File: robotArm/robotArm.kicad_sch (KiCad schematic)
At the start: 30 parts, among them J1 Barrel_Jack, J2 Conn_01x16_Pin, J3 Conn_01x04, J4 Conn_01x04, J5 Conn_01x04, J6 Conn_01x04, U2 TMC2209_SILENTSTEPSTICK, U4 TMC2209_SILENTSTEPSTICK, U5 TMC2209_SILENTSTEPSTICK, U6 74HC165

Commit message: First Real Cleanup
First real cleanup
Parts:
- removed D1: DIAG1, LED_THT:LED_D3.0mm_FlatTop, symbol Device:LED
- removed D2: DIAG2, LED_THT:LED_D3.0mm_FlatTop, symbol Device:LED
- removed D3: DIAG3, LED_THT:LED_D3.0mm_FlatTop, symbol Device:LED
- removed D4: DIAG4, LED_THT:LED_D3.0mm_FlatTop, symbol Device:LED
- removed D5: IX1, LED_THT:LED_D3.0mm_FlatTop, symbol Device:LED
- removed D6: IX2, LED_THT:LED_D3.0mm_FlatTop, symbol Device:LED
- removed D7: IX3, LED_THT:LED_D3.0mm_FlatTop, symbol Device:LED
- removed D8: IX4, LED_THT:LED_D3.0mm_FlatTop, symbol Device:LED
- removed J2: Conn_01x16_Pin, Connector_PinHeader_2.54mm:PinHeader_1x16_P2.54mm_Vertical, symbol Connector:Conn_01x16_Pin
- removed R1: R, Resistor_THT:R_Axial_DIN0204_L3.6mm_D1.6mm_P2.54mm_Vertical, symbol Device:R
- removed R2: R, Resistor_THT:R_Box_L8.4mm_W2.5mm_P5.08mm, symbol Device:R
- removed R3, R4, R5, R6, R7, R8, R9: 330, Resistor_THT:R_Box_L8.4mm_W2.5mm_P5.08mm, symbol Device:R
- removed U6: 74HC165, Package_DIP:DIP-16_W7.62mm, symbol 74xx:74HC165
- J3: value Conn_01x04 -> STEPPER1
- J5: value Conn_01x04 -> STEPPER2
- J6: value Conn_01x04 -> STEPPER3
- U1, U2: symbol TMC2209_SILENTSTEPSTICK:TMC2209_SILENTSTEPSTICK -> Robot_Controller:Module_TMC2209
- U4: value TMC2209_SILENTSTEPSTICK -> TMC2209_MODULE; symbol TMC2209_SILENTSTEPSTICK:TMC2209_SILENTSTEPSTICK -> Robot_Controller:Module_TMC2209
- U5: value TMC2209_SILENTSTEPSTICK -> TMC2209 Module; symbol TMC2209_SILENTSTEPSTICK:TMC2209_SILENTSTEPSTICK -> Robot_Controller:Module_TMC2209
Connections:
- net +3.3V: no longer U2.15 (MS1), U4.14 (MS2), U4.15 (MS1), U5.14 (MS2)
- net EN_DRV: no longer U1.16 (~{EN}), U2.16 (~{EN}), U4.16 (~{EN}), U5.16 (~{EN})
- net GND: no longer U2.1 (GND), U2.7 (GND)
- net B1-DRV4: now reaches J4.4 (2B)
- net B1-DRV4: now also U4.4 (B1); no longer U4.3 (M1B)
- removed net DIAG1: U1.18 (DIAG)
- removed net DIAG2: U5.18 (DIAG)
- removed net DIAG3: U2.18 (DIAG)
- removed net DIAG4: U4.18 (DIAG)
- removed net IX1: U1.17 (INDEX)
- removed net IX2: U5.17 (INDEX)
- removed net IX3: U2.17 (INDEX)
- removed net IX4: U4.17 (INDEX)
- net M1-1A renamed A1-DRV1
- net A1-DRV1: now also U1.5 (A1); no longer U1.4 (M1A)
- net M1-1B renamed B1-DRV1
- net B1-DRV1: now also U1.4 (B1); no longer U1.3 (M1B)
- net M1-2A renamed A2-DRV1
- net A2-DRV1: now also U1.6 (A2); no longer U1.5 (M2A)
- net M1-2B renamed B2-DRV1
- net B2-DRV1: now also U1.3 (B2); no longer U1.6 (M2B)
- net M2-1A renamed A1-DRV2
- net A1-DRV2: now also U5.5 (A1); no longer U5.4 (M1A)
- net M2-1B renamed B1-DRV2
- net B1-DRV2: now also U5.4 (B1); no longer U5.3 (M1B)
- net M2-2A renamed A2-DRV2
- net A2-DRV2: now also U5.6 (A2); no longer U5.5 (M2A)
- net M2-2B renamed B2-DRV2
- net B2-DRV2: now also U5.3 (B2); no longer U5.6 (M2B)
- net M3-1A renamed A1-DRV3
- net A1-DRV3: now also U2.5 (A1); no longer U2.4 (M1A)
- net M3-1B renamed B1-DRV3
- net B1-DRV3: now also U2.4 (B1); no longer U2.3 (M1B)
- net M3-2A renamed A2-DRV3
- net A2-DRV3: now also U2.6 (A2); no longer U2.5 (M2A)
- net M3-2B renamed B2-DRV3
- net B2-DRV3: now also U2.3 (B2); no longer U2.6 (M2B)
- net M4-1A renamed A1-DRV4
- net A1-DRV4: now also U4.5 (A1); no longer U4.4 (M1A)
- net M4-1B renamed A2-DRV4
- net A2-DRV4: now also J4.2 (1A); no longer J4.1 (1B)
- removed net M4-2A: J4.2 (1A), U4.5 (M2A)
- new net: U2.1 (GND), U2.7 (GND)
- new net B2-DRV4: J4.1 (1B), U4.3 (B2)
- new net EN_DRV1: U1.16 (EN)
- new net EN_DRV2: U5.16 (EN)
- new net EN_DRV3: U2.16 (EN)
- new net EN_DRV4: U4.16 (EN)
- no-connect marks 27 -> 18
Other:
- added sheet Endstop Section (endstop_section.kicad_sch)
- company: (none) -> Turnimator Cyberdelix - Jan Atle Ramsli
- title: (none) -> Robot Control Board
- moved on the sheet: J3, J4, J5, J6, U7

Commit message: Attempt 2.1
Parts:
- added C4: 100μ, Capacitor_THT:CP_Radial_D7.5mm_P2.50mm, symbol Device:C
- added D9: LED, LED_THT:LED_D5.0mm_Clear, symbol Device:LED
- added J2: ENDSTOP INPUTS, Connector_PinHeader_2.54mm:PinHeader_1x16_P2.54mm_Vertical, symbol Connector:Conn_01x16_Pin
- added R1: 470 Ω, Resistor_THT:R_Axial_DIN0207_L6.3mm_D2.5mm_P2.54mm_Vertical, symbol Device:R
- added SW1: SW_DIP_x08, Package_DIP:DIP-16_W7.62mm, symbol Switch:SW_DIP_x08
- added SW2: SW_SPDT, SS-12D10G5_XKB, symbol 2026-09-22_07-48-55:SS-12D10G5
- J4: value Conn_01x04 -> STEPPER4
- U7: footprint ESP32_30pin -> Library:ESP32_30pin
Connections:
- net +12V: now also R1.1, SW2.2; no longer J1.1
- net +3.3V: now also C4.1, SW1.1, SW1.2, SW1.3, SW1.4, SW1.5, SW1.6, SW1.7, SW1.8
- net GND: now also U1.11 (CLK), U2.1 (GND), U2.11 (CLK), U2.7 (GND), U4.11 (CLK), U5.11 (CLK), C4.2, D9.2 (A), J2.10 (Pin_10), J2.12 (Pin_12), J2.14 (Pin_14), J2.16 (Pin_16), J2.2 (Pin_2), J2.4 (Pin_4), J2.6 (Pin_6), J2.8 (Pin_8)
- net MS1-DRV4: now reaches U4.14 (MS2)
- net MS1-DRV4: now also SW1.10
- net MS2-DRV4: now reaches U4.15 (MS1)
- net MS2-DRV4: now also SW1.9
- net MS2-DRV2: now reaches U5.14 (MS2)
- net MS2-DRV2: now also SW1.13
- net MS1-DRV2: now reaches U5.15 (MS1)
- net MS1-DRV2: now also SW1.14
- net MS2-DRV1: now reaches U1.14 (MS2)
- net MS2-DRV1: now also SW1.15
- net MS1-DRV1: now reaches U1.15 (MS1)
- net MS1-DRV1: now also SW1.16
- net MS2-DRV3: now reaches U2.14 (MS2)
- net MS2-DRV3: now also SW1.11
- net MS1-DRV3: now reaches U2.15 (MS1)
- net MS1-DRV3: now also SW1.12
- net EN_DRV renamed RESET_DRV
- removed net UART2_TX: U1.12 (TX), U2.12 (TX), U4.12 (TX), U5.12 (TX), U7.22 (GPIO17)
- new net: D9.1 (K), R1.2
- new net: J1.1, SW2.1
- new net Endstop Section/ES0: J2.1 (Pin_1)
- new net Endstop Section/ES1: J2.3 (Pin_3)
- new net Endstop Section/ES2: J2.5 (Pin_5)
- new net Endstop Section/ES3: J2.7 (Pin_7)
- new net Endstop Section/USR0: J2.9 (Pin_9)
- new net Endstop Section/USR1: J2.11 (Pin_11)
- new net Endstop Section/USR2: J2.13 (Pin_13)
- new net Endstop Section/USR3: J2.15 (Pin_15)
- no-connect marks 18 -> 24
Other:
- sheet Endstop Section ports: added ES0, ES1, ES2, ES3, RESET_DRV, USR0, USR1, USR2, USR3; removed none
- note added: "Endstop switches ES0->D0, ES1->D1 ... USR3->D7"
- moved on the sheet: J1

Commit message: JLCPCB READY
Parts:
- removed SW2: SW_SPDT, SS-12D10G5_XKB, symbol 2026-09-22_07-48-55:SS-12D10G5
- added C6: 100µF 100V, Capacitor_THT:CP_Radial_D12.5mm_P2.50mm, symbol Device:C
- added SW2: ~, symbol K23D05_G6:2P3T
- SW1: footprint Package_DIP:DIP-16_W7.62mm -> Button_Switch_THT:SW_DIP_SPSTx08_Slide_6.7x21.88mm_W7.62mm_P2.54mm_LowProfile
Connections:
- net +12V: now also C6.1, SW2.2
- net GND: now also C6.2
- net at J1.1: now also SW2.1 (Common)
- no-connect marks 24 -> 29
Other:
- moved on the sheet: C4, D9, J1, J2, J3, R1, SW1, U1, U7, U8

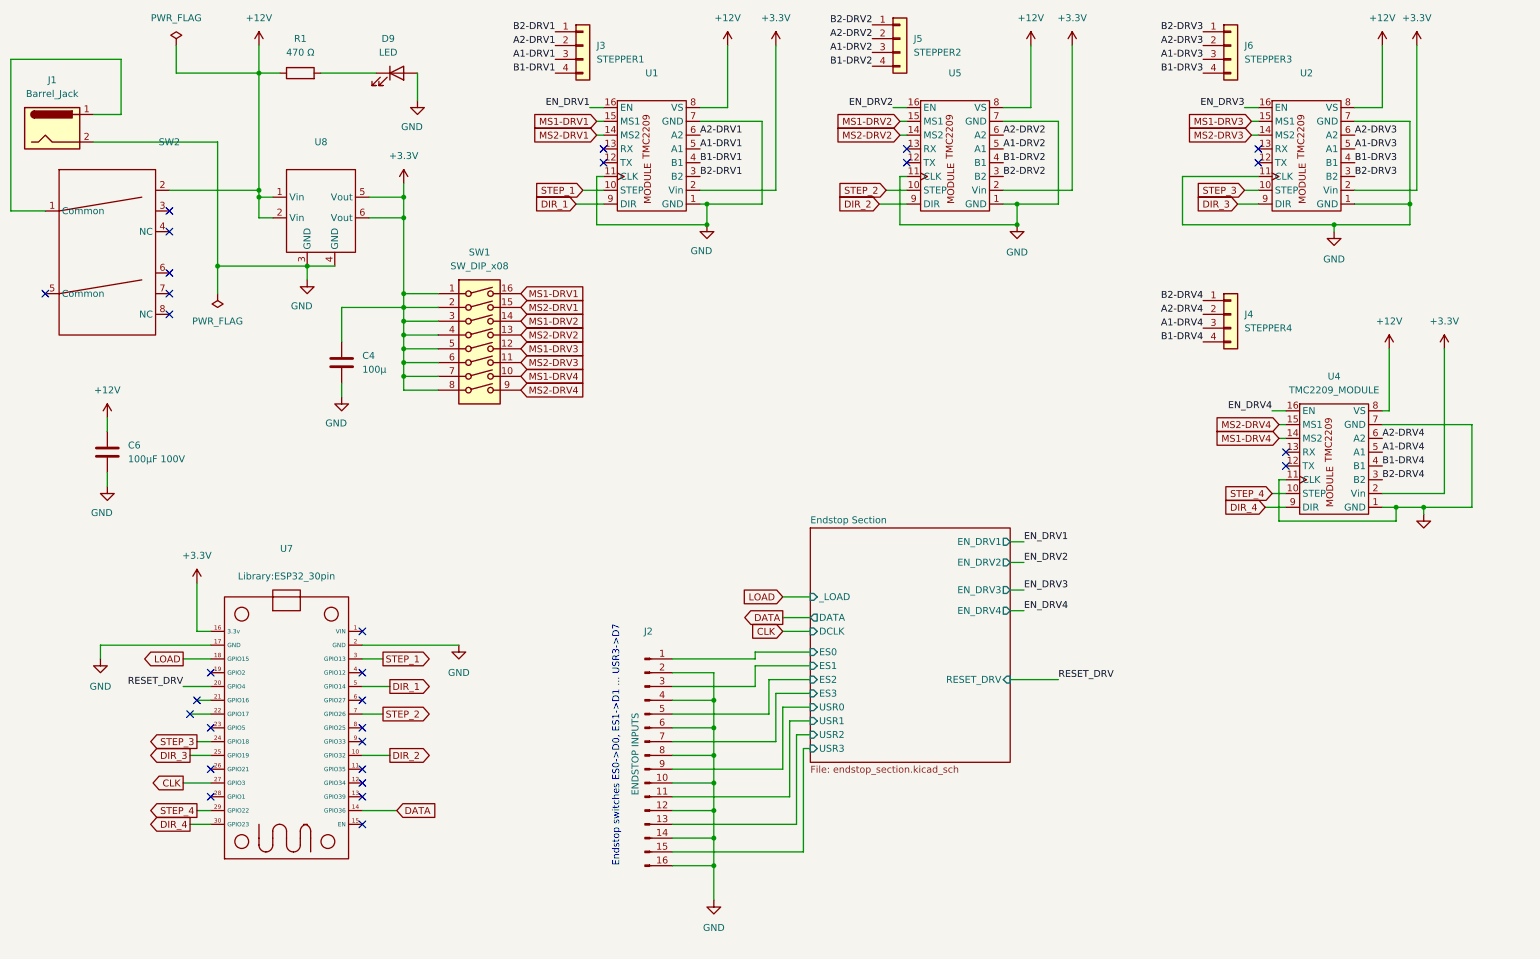
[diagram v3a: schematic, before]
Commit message: Moved switch off board.
I send this off to JLCPCB.
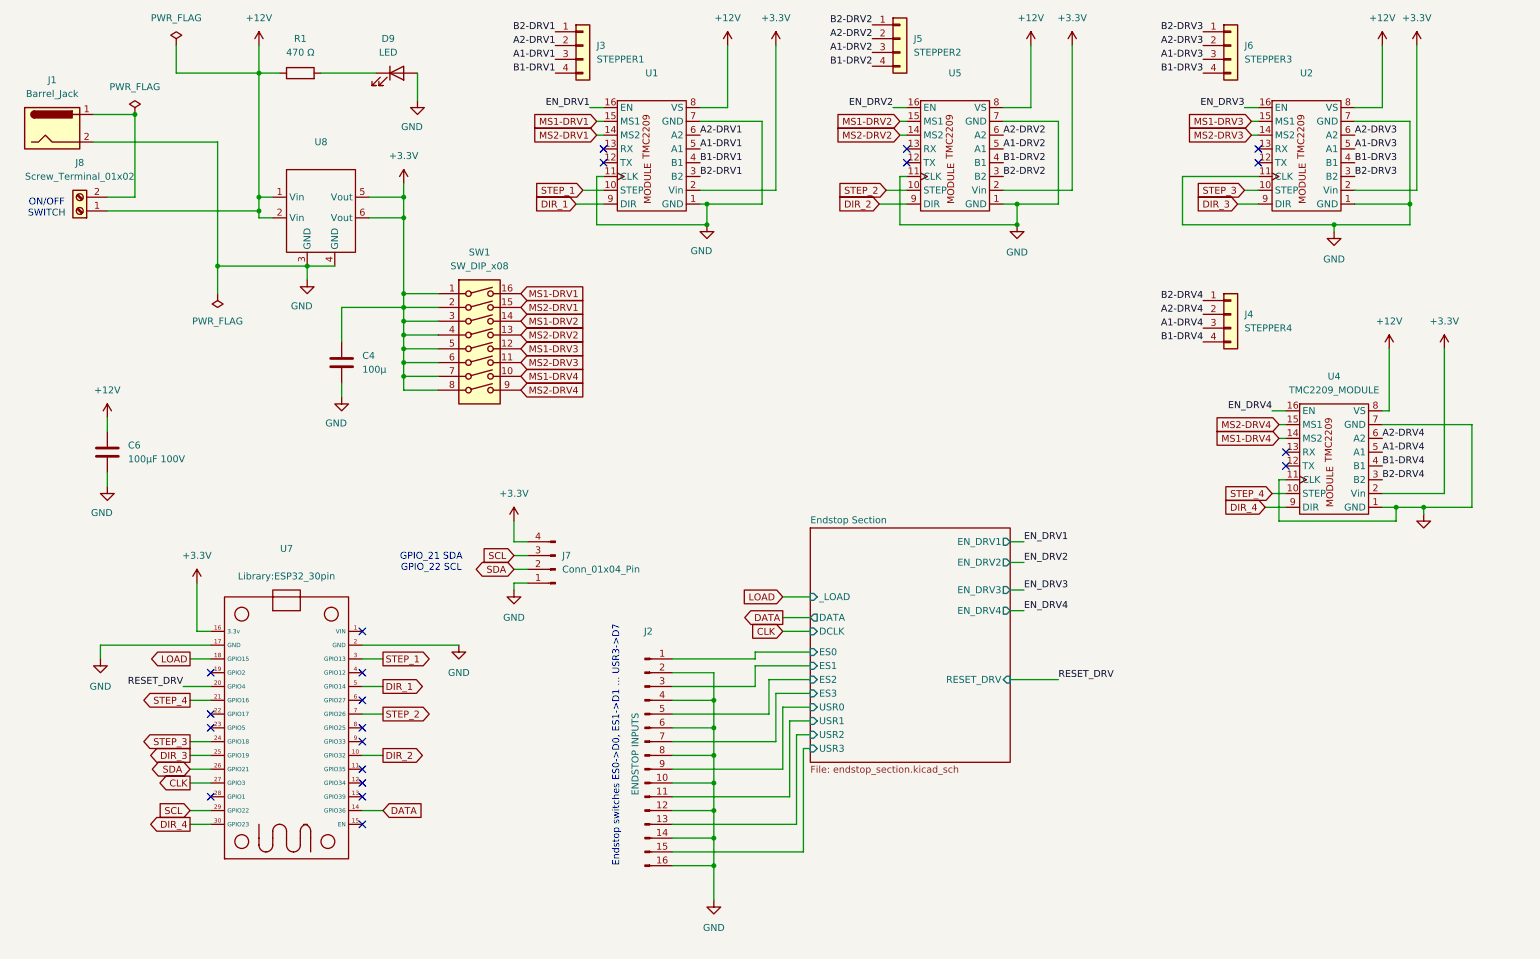
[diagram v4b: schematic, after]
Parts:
- removed SW2: ~, symbol K23D05_G6:2P3T
- added J7: Conn_01x04_Pin, Connector_PinHeader_1.00mm:PinHeader_1x04_P1.00mm_Horizontal, symbol Connector:Conn_01x04_Pin
- added J8: Screw_Terminal_01x02, TerminalBlock_Phoenix:TerminalBlock_Phoenix_MKDS-1,5-2_1x02_P5.00mm_Horizontal, symbol Connector:Screw_Terminal_01x02
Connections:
- net +12V: now also J8.1 (Pin_1)
- net +3.3V: now also J7.4 (Pin_4)
- net GND: now also J7.1 (Pin_1)
- net STEP_4: now also U7.21 (GPIO16); no longer U7.29 (GPIO22)
- net SDA: now reaches U7.26 (GPIO21)
- net SDA: now also J7.2 (Pin_2)
- net at J1.1: now also J8.2 (Pin_2)
- new net SCL: J7.3 (Pin_3), U7.29 (GPIO22)
- no-connect marks 29 -> 21
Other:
- note added: "GPIO_21 SDA GPIO_22 SCL"
- note added: "ON/OFF SWITCH"

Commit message: Added END-EFFECTOR
Not yet sent to JLCPCB
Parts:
- added J9: END EFFECTOR, Connector_PinHeader_2.54mm:PinHeader_2x05_P2.54mm_Vertical, symbol Connector_Generic:Conn_02x05_Counter_Clockwise
- C6: footprint Capacitor_THT:CP_Radial_D12.5mm_P2.50mm -> Capacitor_THT:C_Radial_D6.3mm_H11.0mm_P2.50mm
- J7: footprint Connector_PinHeader_1.00mm:PinHeader_1x04_P1.00mm_Horizontal -> Connector_PinHeader_2.54mm:PinHeader_1x04_P2.54mm_Vertical
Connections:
- net +3.3V: now also J9.1 (Pin_1)
- net GND: now also J9.10 (Pin_10), J9.2 (Pin_2), J9.4 (Pin_4), J9.6 (Pin_6), J9.8 (Pin_8)
- net GPIO17: now reaches U7.22 (GPIO17)
- net GPIO17: now also J9.3 (Pin_3)
- net GPIO27: now reaches U7.6 (GPIO27)
- net GPIO27: now also J9.7 (Pin_7)
- net GPIO25: now reaches U7.8 (GPIO25)
- net GPIO25: now also J9.5 (Pin_5)
- net GPIO33: now reaches U7.9 (GPIO33)
- net GPIO33: now also J9.9 (Pin_9)
- no-connect marks 21 -> 17
